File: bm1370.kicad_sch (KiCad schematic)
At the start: 49 parts, among them U5 MCP1824T-1202E/OT, U6 MCP1824T-0802E, U7 25MHz, U8 BM1370_mode1, U9 SN74AVC4T774

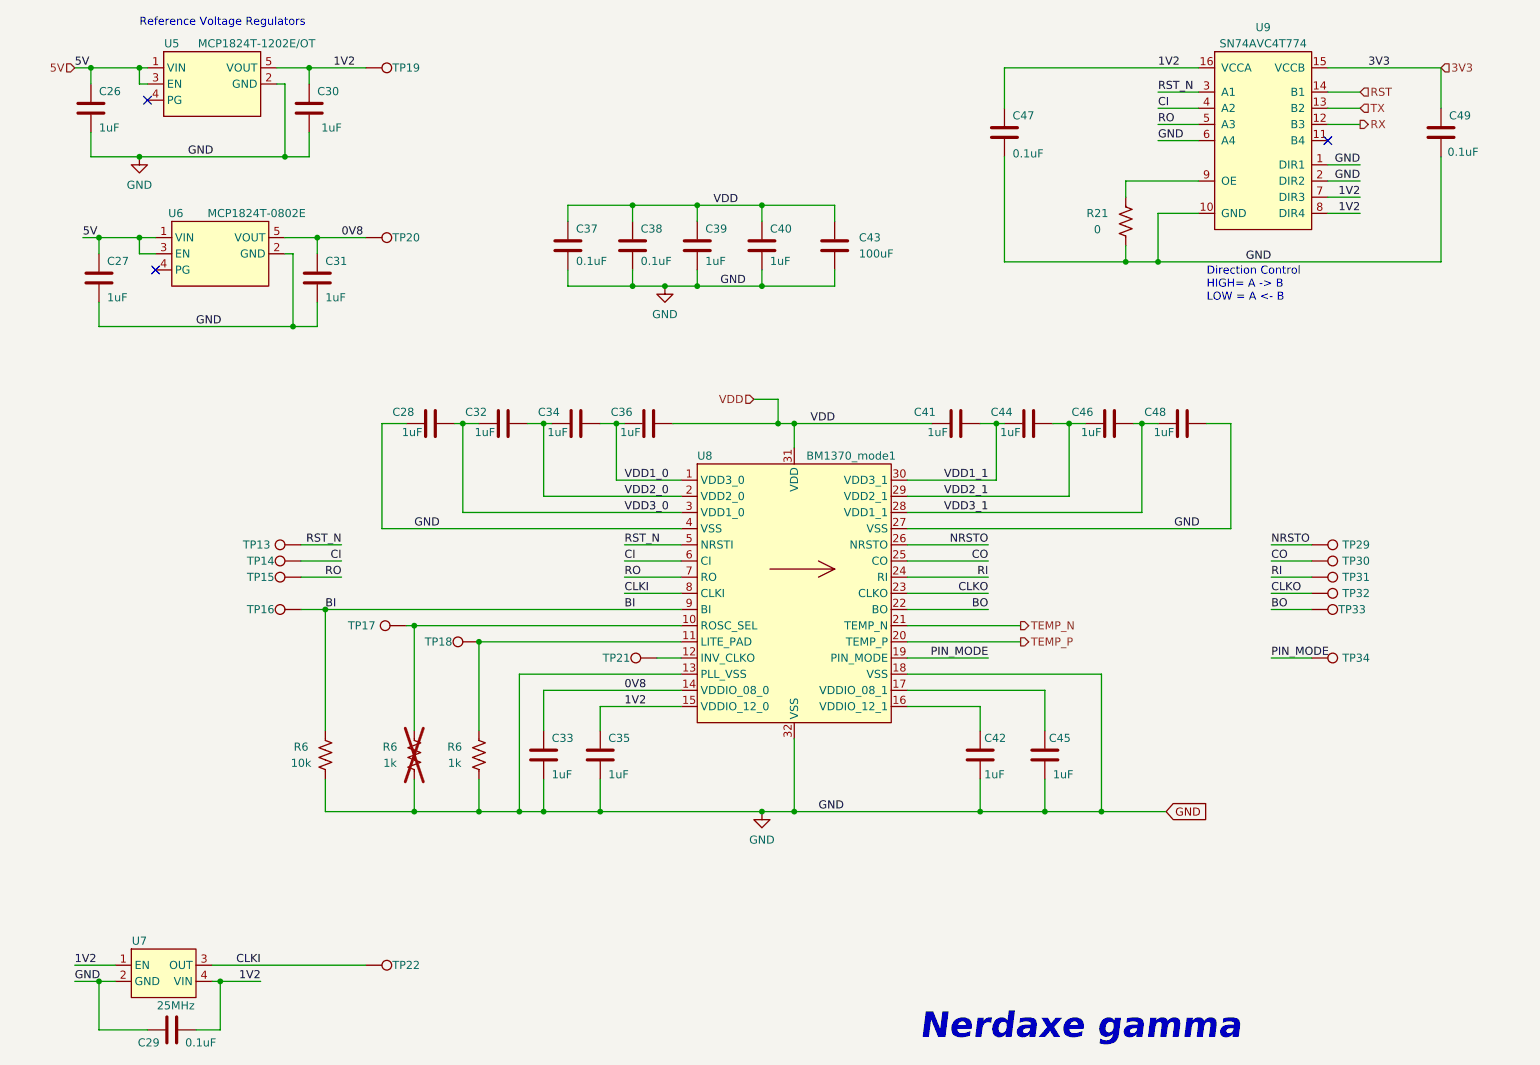
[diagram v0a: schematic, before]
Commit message: Nerdaxe Gamma v2.3
- Fix Emi CE needs
- Added ferrite beads + EMI blocking capacitors
- New components added: R16, R20, R26, R27C21, C22, C23, FB1, FB2, FB3, FB4, FB5, FB6
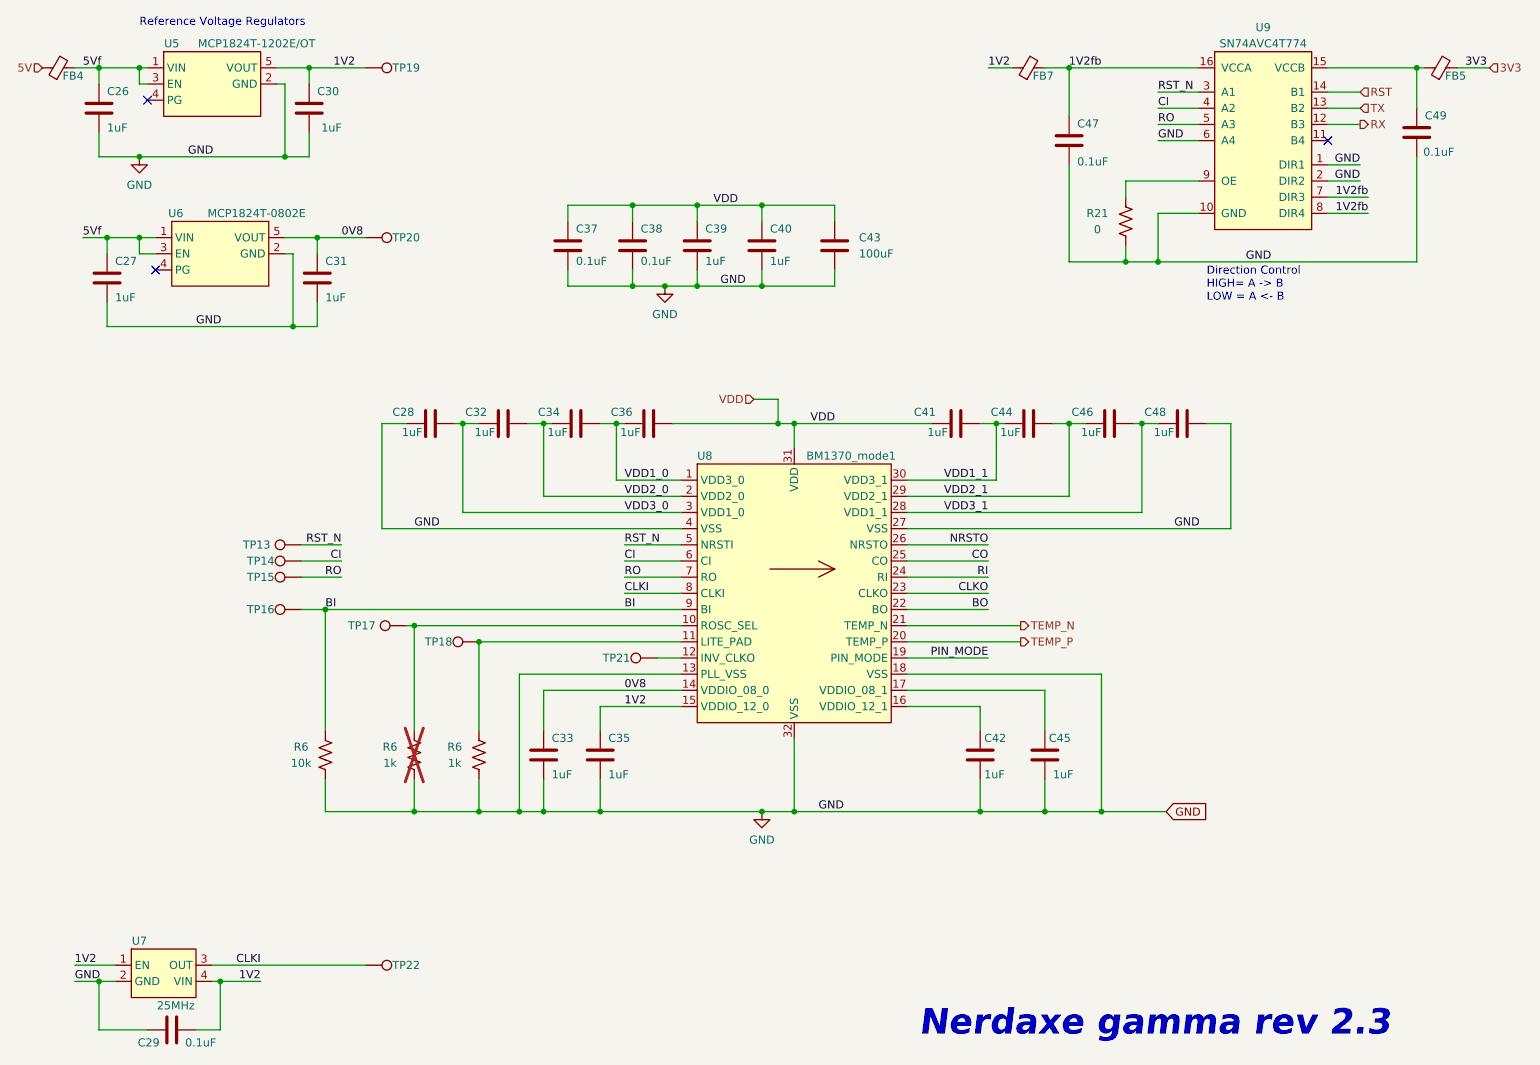
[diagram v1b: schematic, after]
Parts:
- removed TP29, TP30, TP31, TP32, TP33, TP34: TestPoint, TestPoint:TestPoint_Pad_D1.5mm, symbol Connector:TestPoint
- added FB4, FB5, FB7: BLM21PG221SN1D, Resistor_SMD:R_0805_2012Metric, symbol Device:FerriteBead_Small
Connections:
- net 1V2: now also FB7.1; no longer C47.1, U9.16 (VCCA), U9.7 (DIR3), U9.8 (DIR4)
- net 3V3: now also FB5.2; no longer C49.1, U9.15 (VCCB)
- net 5V: now also FB4.1; no longer C26.1, C27.1, U5.1 (VIN), U5.3 (EN), U6.1 (VIN), U6.3 (EN)
- new net: C49.1, FB5.1, U9.15 (VCCB)
- new net 1V2fb: C47.1, FB7.2, U9.16 (VCCA), U9.7 (DIR3), U9.8 (DIR4)
- new net 5Vf: C26.1, C27.1, FB4.2, U5.1 (VIN), U5.3 (EN), U6.1 (VIN), U6.3 (EN)
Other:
- note added: "Nerdaxe gamma rev 2.3"
- note removed: "Nerdaxe gamma"
- moved on the sheet: C26, C27, C47, C49
